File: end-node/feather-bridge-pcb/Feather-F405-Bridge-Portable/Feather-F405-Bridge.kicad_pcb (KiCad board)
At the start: 2 copper layers, 39.6 x 66.3 mm, 12 parts, among them J1 Conn_01x06, J2 Conn_02x02_Odd_Even, J3 Conn_01x03, J4 Conn_01x07, SW1 B3F-3152, SW2 TL1105MF160Q, SW3 TL1105MF160Q, SW4 ELUMEETHQ7C22, U1 LoRa Radio FeatherWing

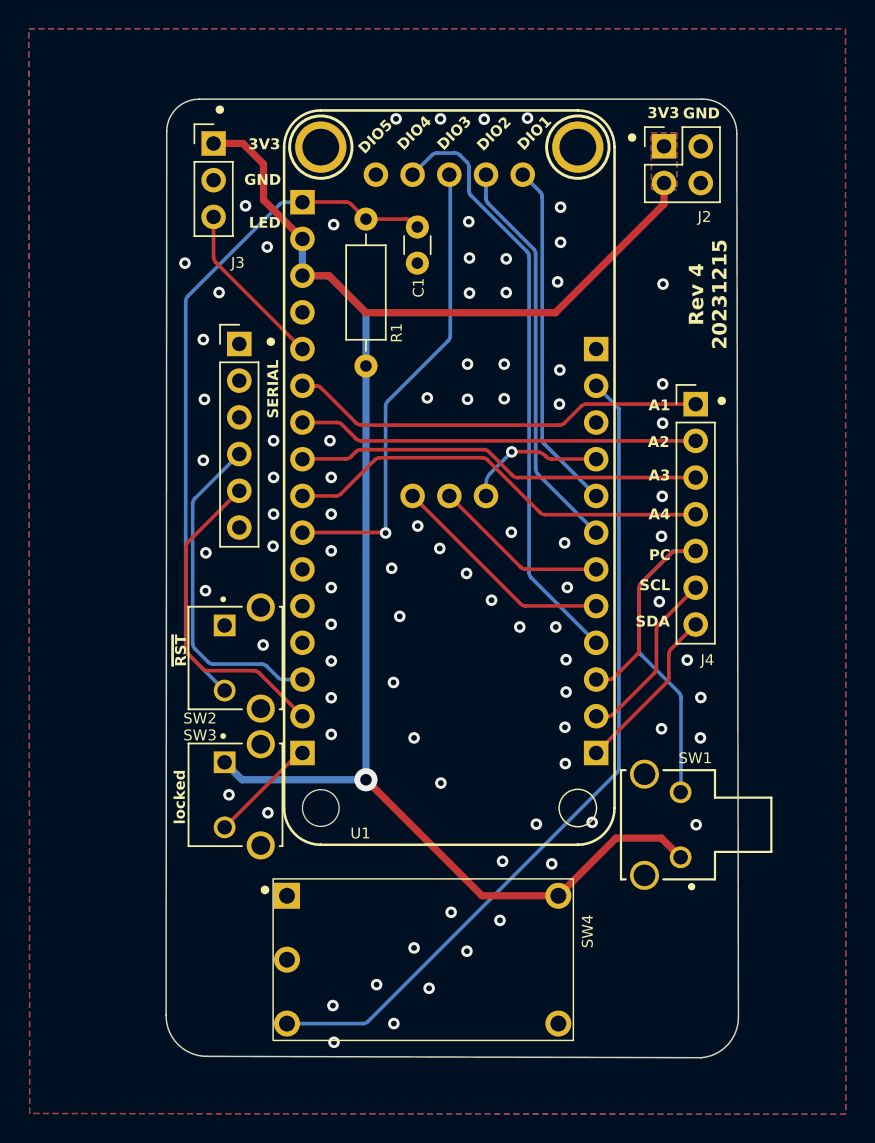
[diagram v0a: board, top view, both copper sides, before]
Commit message: changed receptacle pins from 315 to 801 series
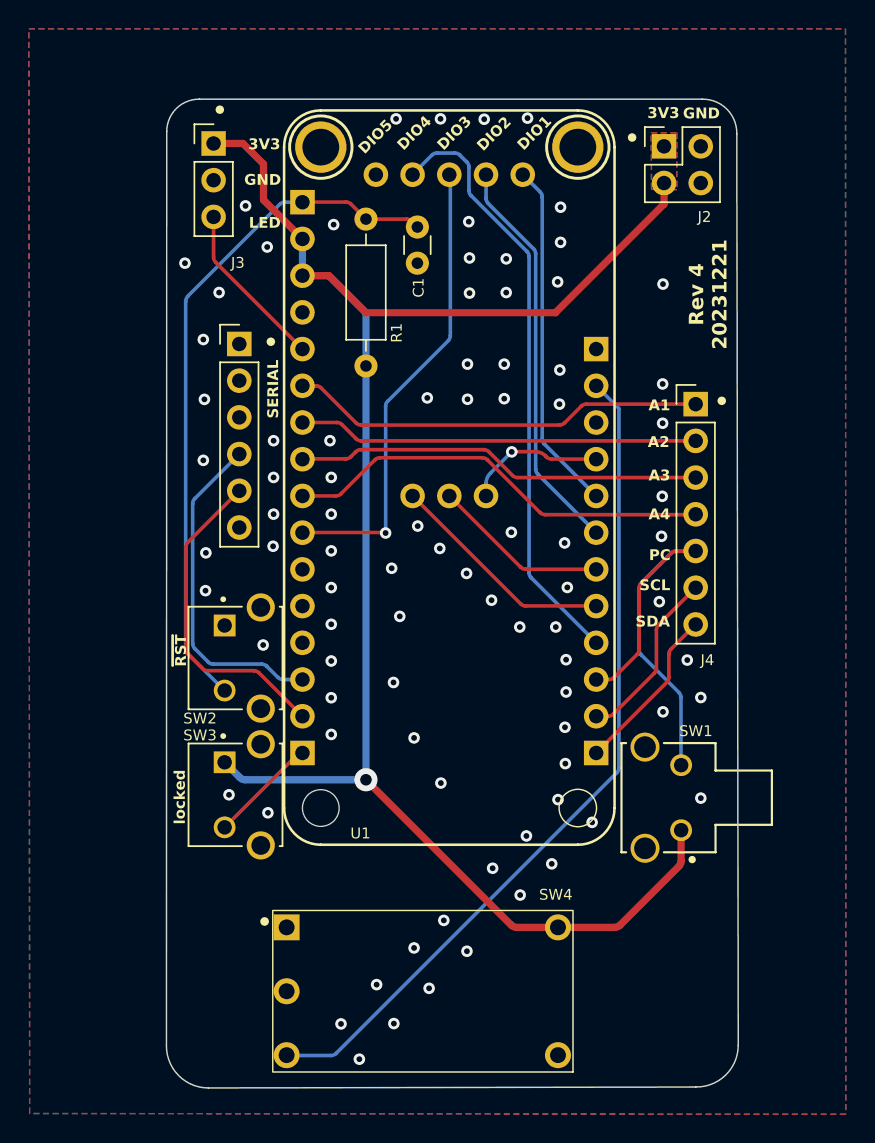
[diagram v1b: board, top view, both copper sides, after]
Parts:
- moved SW4 2.18 mm to (80.6, 158.8)
- moved SW1 1.87 mm to (80.0, 168.0)
- moved REF** 1.49 mm to (47.8, 182.6)
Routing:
- net 3V3: track 118.7 -> 121.5 mm
- net PC_BUTTON: track 33.5 -> 31.6 mm
- net REG3V3_EN: track 57.4 -> 58.4 mm
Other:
- board size 39.6 x 66.3 mm -> 39.6 x 68.4 mm
- board text added: "Rev 4 20231221"
- board text removed: "Rev 4 20231215"
